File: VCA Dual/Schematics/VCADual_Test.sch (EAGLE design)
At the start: 49 parts, among them IC1 QUAD_OPAMPD, IC2 SSM2164S, IC4 TL072D, IC5 TL074D, IC6 TL072D

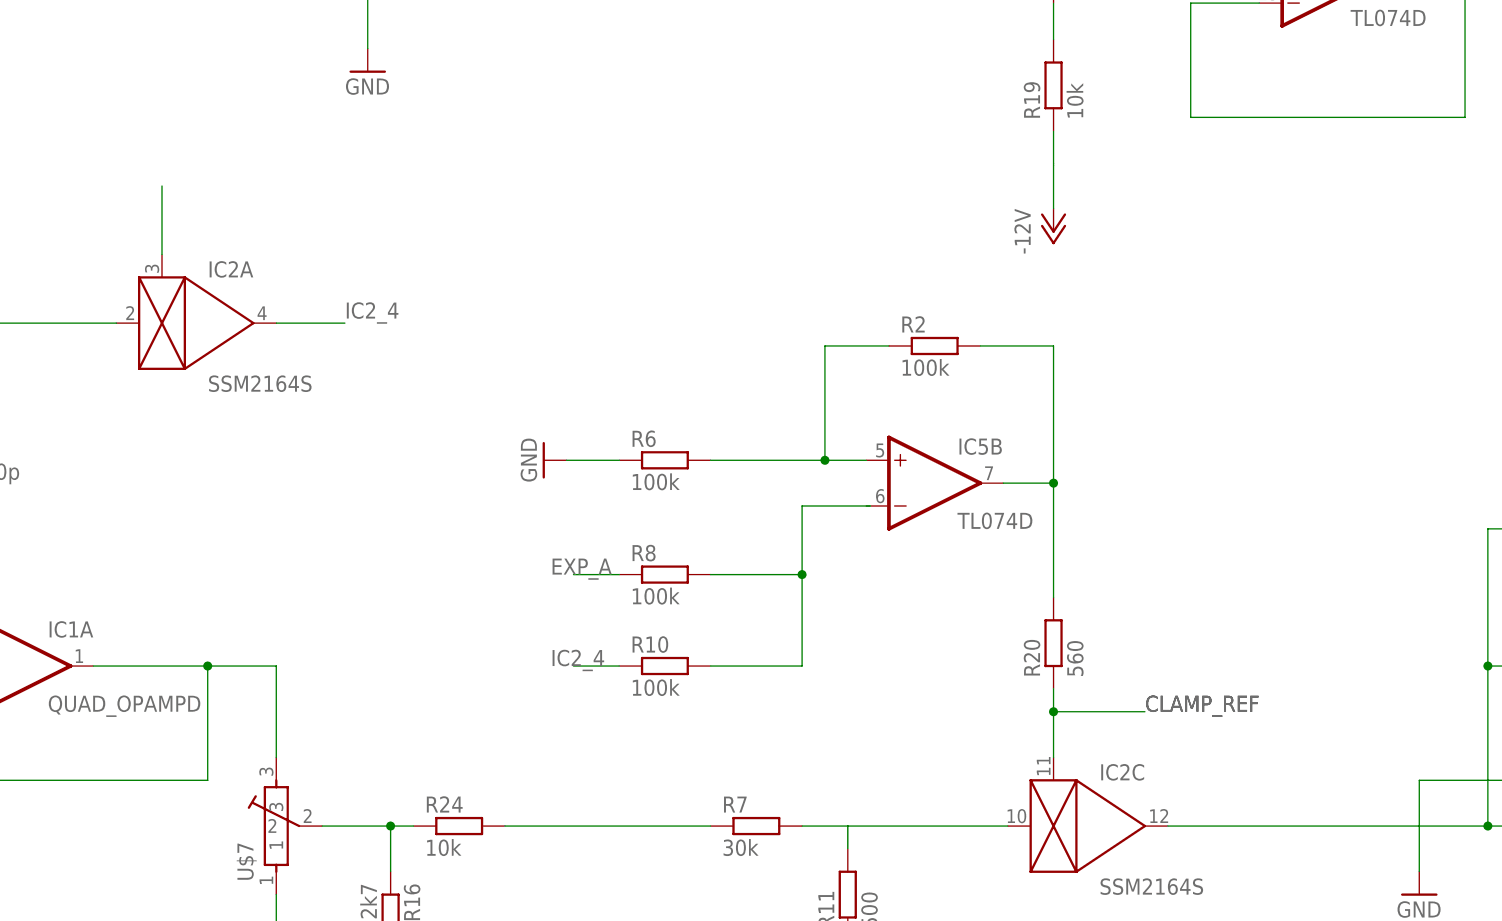
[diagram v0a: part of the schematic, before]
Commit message: Added Clamp Diode
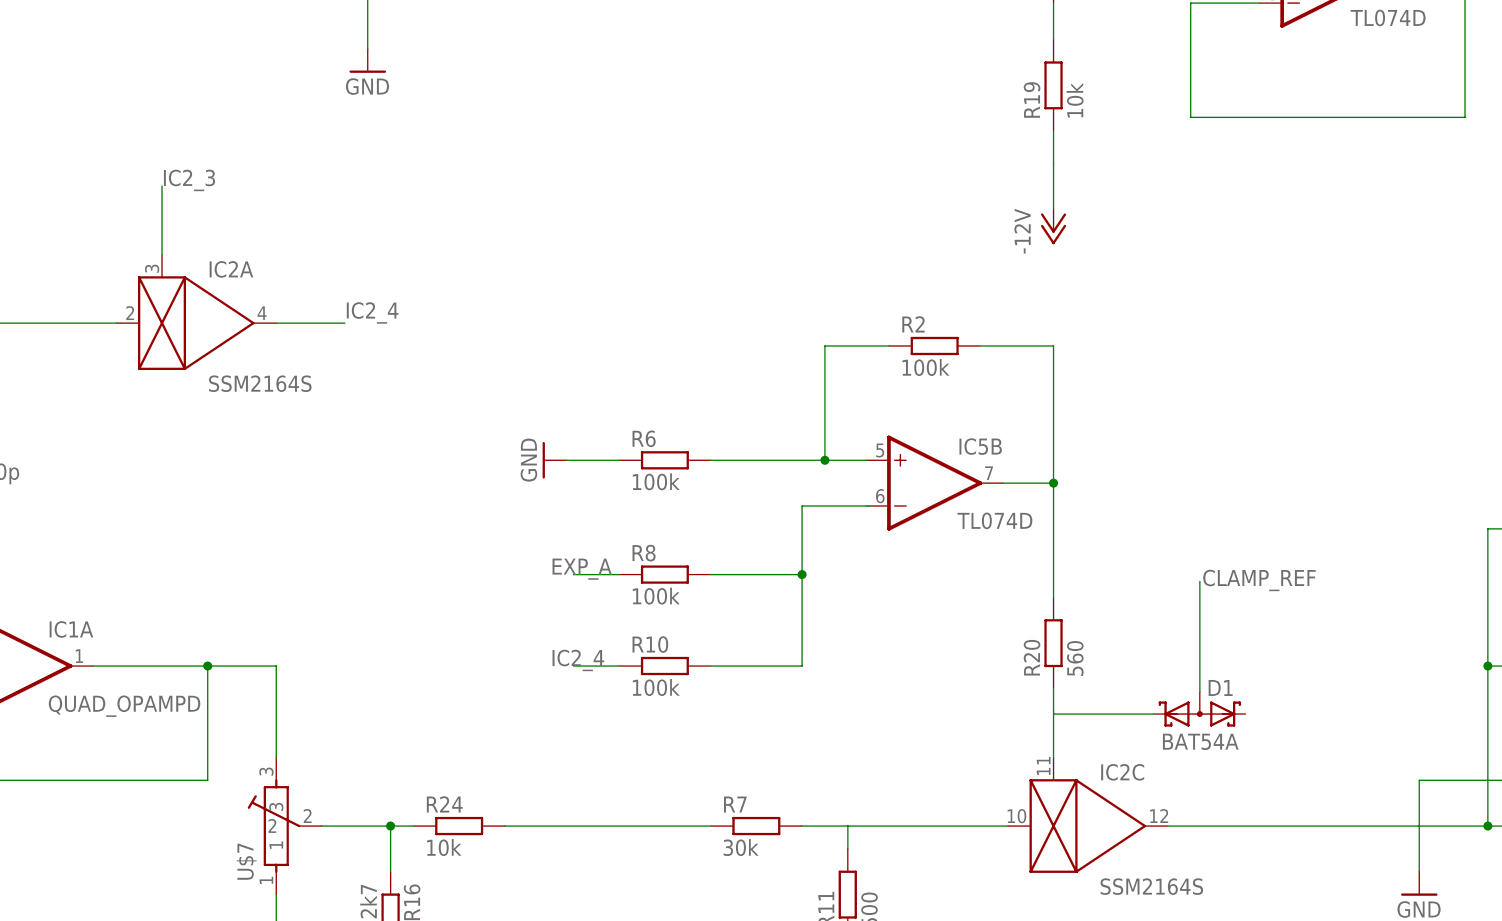
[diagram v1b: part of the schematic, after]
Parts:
- added D1: BAT54A, diode:BAT54A
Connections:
- net CLAMP_REF: now also D1.AA, D1.K1
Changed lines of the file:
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@@
 <?xml version="1.0" encoding="utf-8"?>
 <!DOCTYPE eagle SYSTEM "eagle.dtd">
-<eagle version="7.6.0">
+<eagle version="8.0.0">
 <drawing>
 <settings>
@@
 <part name="P-1" library="supply1" deviceset="-12V" device=""/>
 <part name="R20" library="Rebel" deviceset="R-EU_" device="0603" value="560"/>
+<part name="D1" library="diode" deviceset="BAT54A" device=""/>
 </parts>
 <sheets>
@@
 <instance part="P-1" gate="1" x="-198.12" y="-60.96"/>
 <instance part="R20" gate="G$1" x="-198.12" y="-106.68" rot="R90"/>
+<instance part="D1" gate="G$1" x="-181.864" y="-114.554"/>
 </instances>
 <busses>
@@
 <pinref part="IC2" gate="A" pin="CTRL"/>
 <wire x1="-297.18" y1="-63.5" x2="-297.18" y2="-55.88" width="0.1524" layer="91"/>
+<label x="-297.18" y="-55.88" size="1.778" layer="95"/>
 </segment>
 </net>
@@
 <pinref part="IC2" gate="C" pin="CTRL"/>
 <pinref part="R20" gate="G$1" pin="1"/>
-<wire x1="-198.12" y1="-119.38" x2="-198.12" y2="-114.3" width="0.1524" layer="91"/>
+<wire x1="-198.12" y1="-119.38" x2="-198.12" y2="-114.554" width="0.1524" layer="91"/>
+<pinref part="D1" gate="G$1" pin="K1"/>
 <wire x1="-198.12" y1="-114.3" x2="-198.12" y2="-111.76" width="0.1524" layer="91"/>
-<wire x1="-198.12" y1="-114.3" x2="-187.96" y2="-114.3" width="0.1524" layer="91"/>
-<junction x="-198.12" y="-114.3"/>
-<label x="-187.96" y="-114.3" size="1.778" layer="95"/>
-<label x="-187.96" y="-114.3" size="1.778" layer="95"/>
-</segment>
-</net>
+<wire x1="-186.944" y1="-114.554" x2="-198.12" y2="-114.554" width="0.1524" layer="91"/>
+<wire x1="-198.12" y1="-114.554" x2="-198.12" y2="-114.3" width="0.1524" layer="91"/>
+</segment>
+<segment>
+<pinref part="D1" gate="G$1" pin="AA"/>
+<wire x1="-181.864" y1="-112.014" x2="-181.864" y2="-99.822" width="0.1524" layer="91"/>
+<label x="-181.61" y="-100.33" size="1.778" layer="95"/>
+</segment>
+</net>
